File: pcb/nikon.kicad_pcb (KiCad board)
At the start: 2 copper layers, 143.3 x 124.7 mm, 89 parts, among them J1 USB_C_Receptacle_USB2.0, J2 AVR-ISP-6, J3 SJ2-35043A-SMT-TR, SW1 SW_Push, U1 ATmega32U4-AU, Y1 16MHz

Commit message: pre-flippable
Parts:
- J3: value SJ2-35043A-SMT-TR -> SJ2-35894A-SMT-TR; footprint nikon:CUI_SJ2-35043A-SMT-TR -> nikon:CUI_SJ2-35894A-SMT-TR
- MX20: footprint nikon:SW_Kailh_Choc_V1_1.50u -> nikon:SW_Kailh_Choc_V1_1.00u
- moved SW1 18.1 mm to (137.8, 69.6)
- moved D1 8.50 mm to (27.9, 49.7)
- moved D10 8.50 mm to (44.7, 117.7)
- moved D2 8.50 mm to (27.9, 66.7)
- moved D3 8.50 mm to (27.9, 83.7)
- moved D4 8.50 mm to (27.9, 100.7)
- moved D5 8.50 mm to (27.9, 117.7)
- moved D6 8.50 mm to (44.7, 49.7)
- moved D7 8.50 mm to (44.7, 66.7)
- moved D8 8.50 mm to (44.7, 83.7)
- moved D9 8.50 mm to (44.7, 100.7)
- moved MX1 8.50 mm to (35.7, 44.2)
- moved MX10 8.50 mm to (53.7, 112.2)
- moved MX2 8.50 mm to (35.7, 61.2)
- moved MX3 8.50 mm to (35.7, 78.2)
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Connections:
- J3 pad 1: unconnected-(J3-Pad1) -> GND
- J3 pad 2: unconnected-(J3-Pad2) -> /SCL
- J3 pad 3: unconnected-(J3-Pad3) -> /SDA
- J3 pad 4: unconnected-(J3-Pad4) -> +5V
- U1 pad 18: unconnected-(U1-Pad18) -> /SCL
- U1 pad 19: unconnected-(U1-Pad19) -> /SDA
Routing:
- net /D-: track 71.3 -> 0.00 mm
- net /D+: track 69.7 -> 0.00 mm
- net GND: track 27.8 -> 0.00 mm
- net +5V: track 27.0 -> 0.00 mm, vias 2 -> 0
- net Net-(J1-PadB5): track 16.2 -> 0.00 mm, vias 1 -> 0
- net /XTAL1: track 11.7 -> 0.00 mm
- net /XTAL2: track 10.4 -> 0.00 mm
- net /USB_D+: track 10.4 -> 0.00 mm
- net Net-(C1-Pad1): track 9.67 -> 0.00 mm
- net /USB_D-: track 7.61 -> 0.00 mm
- net Net-(F1-Pad2): track 5.77 -> 0.00 mm
- net Net-(D34-Pad2): track 5.27 -> 0.00 mm
- net Net-(D30-Pad2): track 5.26 -> 0.00 mm
- net Net-(D25-Pad2): track 5.25 -> 0.00 mm
- net Net-(J1-PadA5): track 4.50 -> 0.00 mm
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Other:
- board size 143.3 x 124.7 mm -> 143.3 x 128.9 mm

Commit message: ...........
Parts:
- added D35: 1N4148, Diode_SMD:D_SOD-123F, F.Cu at (137.1, 64.6)
- added D36: 1N4148, Diode_SMD:D_SOD-123F, F.Cu at (134.7, 86.4)
- added D37: 1N4148, Diode_SMD:D_SOD-123F, F.Cu at (151.0, 125.3)
- added D38: 1N4148, Diode_SMD:D_SOD-123F, F.Cu at (147.4, 148.6)
- added D39: 1N4148, Diode_SMD:D_SOD-123F, F.Cu at (134.7, 47.6)
- added D40: 1N4148, Diode_SMD:D_SOD-123F, F.Cu at (134.7, 64.6)
- added D41: 1N4148, Diode_SMD:D_SOD-123F, F.Cu at (134.7, 81.6)
- added D42: 1N4148, Diode_SMD:D_SOD-123F, F.Cu at (134.6, 93.8)
- added D43: 1N4148, Diode_SMD:D_SOD-123F, F.Cu at (132.7, 140.1)
- added D44: 1N4148, Diode_SMD:D_SOD-123F, F.Cu at (116.7, 45.4)
- added D45: 1N4148, Diode_SMD:D_SOD-123F, F.Cu at (116.7, 62.4)
- added D46: 1N4148, Diode_SMD:D_SOD-123F, F.Cu at (116.7, 79.4)
- added D47: 1N4148, Diode_SMD:D_SOD-123F, F.Cu at (116.7, 96.4)
- added D48: 1N4148, Diode_SMD:D_SOD-123F, F.Cu at (118.0, 131.6)
- added D49: 1N4148, Diode_SMD:D_SOD-123F, F.Cu at (98.7, 41.2)
- added D50: 1N4148, Diode_SMD:D_SOD-123F, F.Cu at (98.7, 58.2)
- added D51: 1N4148, Diode_SMD:D_SOD-123F, F.Cu at (98.7, 75.2)
- added D52: 1N4148, Diode_SMD:D_SOD-123F, F.Cu at (98.7, 92.2)
- added D53: 1N4148, Diode_SMD:D_SOD-123F, F.Cu at (98.7, 109.2)
- added D54: 1N4148, Diode_SMD:D_SOD-123F, F.Cu at (80.7, 43.3)
- added D55: 1N4148, Diode_SMD:D_SOD-123F, F.Cu at (80.7, 60.3)
- added D56: 1N4148, Diode_SMD:D_SOD-123F, F.Cu at (80.7, 77.3)
- added D57: 1N4148, Diode_SMD:D_SOD-123F, F.Cu at (80.7, 94.3)
- added D58: 1N4148, Diode_SMD:D_SOD-123F, F.Cu at (80.7, 111.3)
- added D59: 1N4148, Diode_SMD:D_SOD-123F, F.Cu at (62.7, 49.7)
- added D60: 1N4148, Diode_SMD:D_SOD-123F, F.Cu at (62.7, 66.7)
- added D61: 1N4148, Diode_SMD:D_SOD-123F, F.Cu at (62.7, 83.7)
- added D62: 1N4148, Diode_SMD:D_SOD-123F, F.Cu at (62.7, 100.7)
- added D63: 1N4148, Diode_SMD:D_SOD-123F, F.Cu at (62.7, 117.7)
- added D64: 1N4148, Diode_SMD:D_SOD-123F, F.Cu at (44.7, 49.7)
- added D65: 1N4148, Diode_SMD:D_SOD-123F, F.Cu at (44.7, 66.7)
- added D66: 1N4148, Diode_SMD:D_SOD-123F, F.Cu at (44.7, 83.7)
- added D67: 1N4148, Diode_SMD:D_SOD-123F, F.Cu at (44.7, 100.7)
- added D68: 1N4148, Diode_SMD:D_SOD-123F, F.Cu at (44.7, 117.7)
- added MX35: MX-NoLED, nikon:SW_Kailh_Choc_V1_1.50u, B.Cu at (143.2, 54.1)
- added MX36: MX-NoLED, nikon:SW_Kailh_Choc_V1_1.50u, B.Cu at (143.2, 81.1)
- added MX37: MX-NoLED, nikon:SW_Kailh_Choc_V1_1.50u, B.Cu at (150.8, 114.8)
- added MX38: MX-NoLED, nikon:SW_Kailh_Choc_V1_1.50u, B.Cu at (147.1, 138.1)
- added MX39: MX-NoLED, nikon:SW_Kailh_Choc_V1_1.00u, B.Cu at (125.7, 42.1)
- added MX40: MX-NoLED, nikon:SW_Kailh_Choc_V1_1.00u, B.Cu at (125.7, 59.1)
- added MX41: MX-NoLED, nikon:SW_Kailh_Choc_V1_1.00u, B.Cu at (125.7, 76.1)
- added MX42: MX-NoLED, nikon:SW_Kailh_Choc_V1_1.00u, B.Cu at (125.7, 93.1)
- added MX43: MX-NoLED, nikon:SW_Kailh_Choc_V1_1.50u, B.Cu at (132.4, 129.6)
- added MX44: MX-NoLED, nikon:SW_Kailh_Choc_V1_1.00u, B.Cu at (107.7, 39.9)
- added MX45: MX-NoLED, nikon:SW_Kailh_Choc_V1_1.00u, B.Cu at (107.7, 56.9)
- added MX46: MX-NoLED, nikon:SW_Kailh_Choc_V1_1.00u, B.Cu at (107.7, 73.9)
- added MX47: MX-NoLED, nikon:SW_Kailh_Choc_V1_1.00u, B.Cu at (107.7, 90.9)
- added MX48: MX-NoLED, nikon:SW_Kailh_Choc_V1_1.50u, B.Cu at (117.6, 121.1)
- added MX49: MX-NoLED, nikon:SW_Kailh_Choc_V1_1.00u, B.Cu at (89.7, 35.7)
- added MX50: MX-NoLED, nikon:SW_Kailh_Choc_V1_1.00u, B.Cu at (89.7, 52.7)
- added MX51: MX-NoLED, nikon:SW_Kailh_Choc_V1_1.00u, B.Cu at (89.7, 69.7)
- added MX52: MX-NoLED, nikon:SW_Kailh_Choc_V1_1.00u, B.Cu at (89.7, 86.7)
- added MX53: MX-NoLED, nikon:SW_Kailh_Choc_V1_1.00u, B.Cu at (89.7, 103.7)
- added MX54: MX-NoLED, nikon:SW_Kailh_Choc_V1_1.00u, B.Cu at (71.7, 37.8)
- added MX55: MX-NoLED, nikon:SW_Kailh_Choc_V1_1.00u, B.Cu at (71.7, 54.8)
- added MX56: MX-NoLED, nikon:SW_Kailh_Choc_V1_1.00u, B.Cu at (71.7, 71.8)
- added MX57: MX-NoLED, nikon:SW_Kailh_Choc_V1_1.00u, B.Cu at (71.7, 88.8)
- added MX58: MX-NoLED, nikon:SW_Kailh_Choc_V1_1.00u, B.Cu at (71.7, 105.8)
- added MX59: MX-NoLED, nikon:SW_Kailh_Choc_V1_1.00u, B.Cu at (53.7, 44.2)
- added MX60: MX-NoLED, nikon:SW_Kailh_Choc_V1_1.00u, B.Cu at (53.7, 61.2)
- added MX61: MX-NoLED, nikon:SW_Kailh_Choc_V1_1.00u, B.Cu at (53.7, 78.2)
- added MX62: MX-NoLED, nikon:SW_Kailh_Choc_V1_1.00u, B.Cu at (53.7, 95.2)
- added MX63: MX-NoLED, nikon:SW_Kailh_Choc_V1_1.00u, B.Cu at (53.7, 112.2)
- added MX64: MX-NoLED, nikon:SW_Kailh_Choc_V1_1.00u, B.Cu at (35.7, 44.2)
- added MX65: MX-NoLED, nikon:SW_Kailh_Choc_V1_1.00u, B.Cu at (35.7, 61.2)
- added MX66: MX-NoLED, nikon:SW_Kailh_Choc_V1_1.00u, B.Cu at (35.7, 78.2)
- added MX67: MX-NoLED, nikon:SW_Kailh_Choc_V1_1.00u, B.Cu at (35.7, 95.2)
- added MX68: MX-NoLED, nikon:SW_Kailh_Choc_V1_1.00u, B.Cu at (35.7, 112.2)
- added R7: 4.7k, Resistor_SMD:R_0805_2012Metric_Pad1.20x1.40mm_HandSolder, F.Cu at (137.9, 69.2)
- added R8: 4.7k, Resistor_SMD:R_0805_2012Metric_Pad1.20x1.40mm_HandSolder, F.Cu at (137.9, 71.5)
- C1, C2, C3, C4, C5, C6, C7, C8, F1, J2, R1, R2, R3, R4, R5, R6, SW1, U1, Y1: moved to F.Cu
- J1: value USB_C_Receptacle_USB2.0 -> USB4105-GF-A; footprint nikon:USB_C_GCT_USB4085 -> nikon:GCT_USB4105-GF-A; moved to F.Cu
- J3: value SJ2-35894A-SMT-TR -> SJ2-35954A-SMT-TR; footprint nikon:CUI_SJ2-35894A-SMT-TR -> nikon:CUI_SJ2-35954A-SMT-TR; moved to F.Cu
- moved J2 49.8 mm to (113.6, 104.0), turned to 180 degrees
- moved SW1 48.4 mm to (103.7, 103.9), turned to 0 degrees
- moved C3 26.0 mm to (121.7, 103.1), turned to 0 degrees
- moved R6 20.1 mm to (140.1, 117.3), turned to 0 degrees
- moved C5 18.1 mm to (125.0, 105.5), turned to -90 degrees
- moved Y1 17.3 mm to (121.7, 109.3), turned to 90 degrees
- moved C7 16.8 mm to (141.8, 113.2), turned to 90 degrees
- moved C1 16.0 mm to (134.0, 98.4), turned to 180 degrees
- moved R1 13.6 mm to (136.0, 37.5), turned to 90 degrees
- moved C4 13.3 mm to (133.1, 100.7), turned to 0 degrees
- moved C2 8.83 mm to (125.0, 112.1), turned to 90 degrees
- moved C8 6.73 mm to (141.8, 106.0), turned to -90 degrees
- moved R4 6.14 mm to (149.0, 37.5), turned to -90 degrees
- moved C6 3.20 mm to (127.7, 117.4), turned to 180 degrees
- moved J1 2.61 mm to (143.2, 27.8), turned to 180 degrees
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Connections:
- net /Col1 renamed /LCol1
- net /Col2 renamed /LCol2
- net /Col3 renamed /LCol3
- net /Col4 renamed /LCol4
- net /Col5 renamed /LCol5
- net /Col6 renamed /LCol6
- net /Col7 renamed /LCol7
- net /Row1 renamed /LRow1
- net /Row2 renamed /LRow2
- net /Row3 renamed /LRow3
- net /Row4 renamed /LRow4
- net /Row5 renamed /LRow5
- J1 pad A5: Net-(J1-PadA5) -> Net-(R4-Pad1)
- R2 pad 1: /D- -> /USB_D-
- R2 pad 2: /USB_D- -> /D-
- R3 pad 1: /D+ -> /USB_D+
- R3 pad 2: /USB_D+ -> /D+
- R4 pad 1: GND -> Net-(R4-Pad1)
- R4 pad 2: Net-(J1-PadA5) -> GND
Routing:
- net /LRow5: track 0.00 -> 140.4 mm
- net /LRow3: track 0.00 -> 123.9 mm, vias 0 -> 2
- net +5V: track 0.00 -> 123.7 mm, vias 0 -> 6
- net /LRow2: track 0.00 -> 122.2 mm
- net /RRow2: track 0.00 -> 101.3 mm
- net /RRow3: track 0.00 -> 100.9 mm
- net /RRow1: track 0.00 -> 99.0 mm
- net /RRow4: track 0.00 -> 99.0 mm
- net /LRow4: track 0.00 -> 97.7 mm
- net /LRow1: track 0.00 -> 97.4 mm
- net /LCol3: track 0.00 -> 77.3 mm, vias 0 -> 8
- net /LCol4: track 0.00 -> 76.2 mm, vias 0 -> 8
- net /LCol2: track 0.00 -> 74.5 mm, vias 0 -> 8
- net /LCol1: track 0.00 -> 74.5 mm
- net /D-: track 0.00 -> 73.1 mm
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- added copper zone on F.Cu, net GND
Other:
- outline, holes or cut-outs redrawn

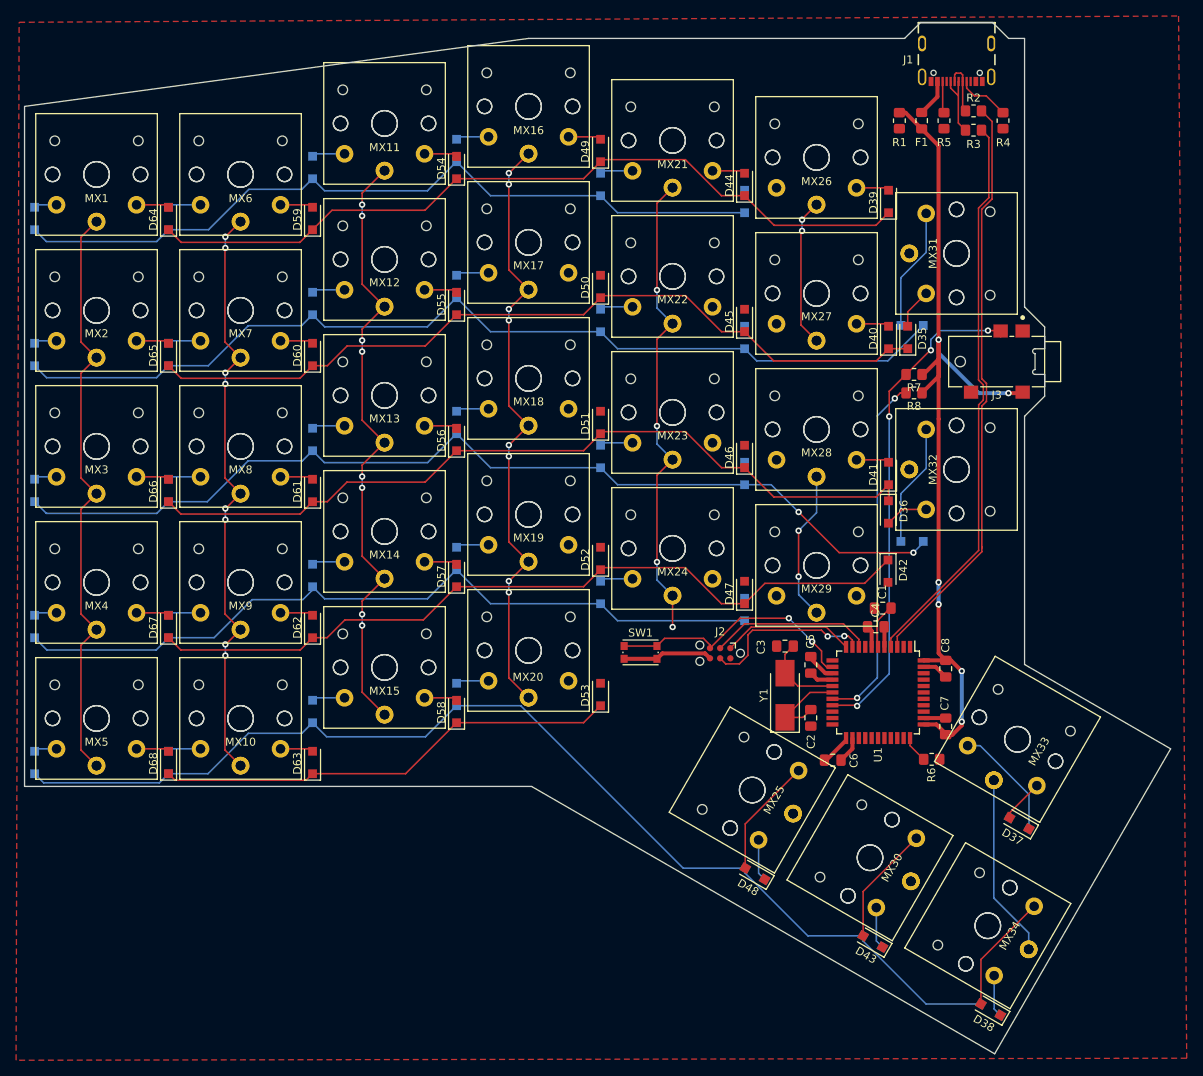
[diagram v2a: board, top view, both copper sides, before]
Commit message: remove right pcb
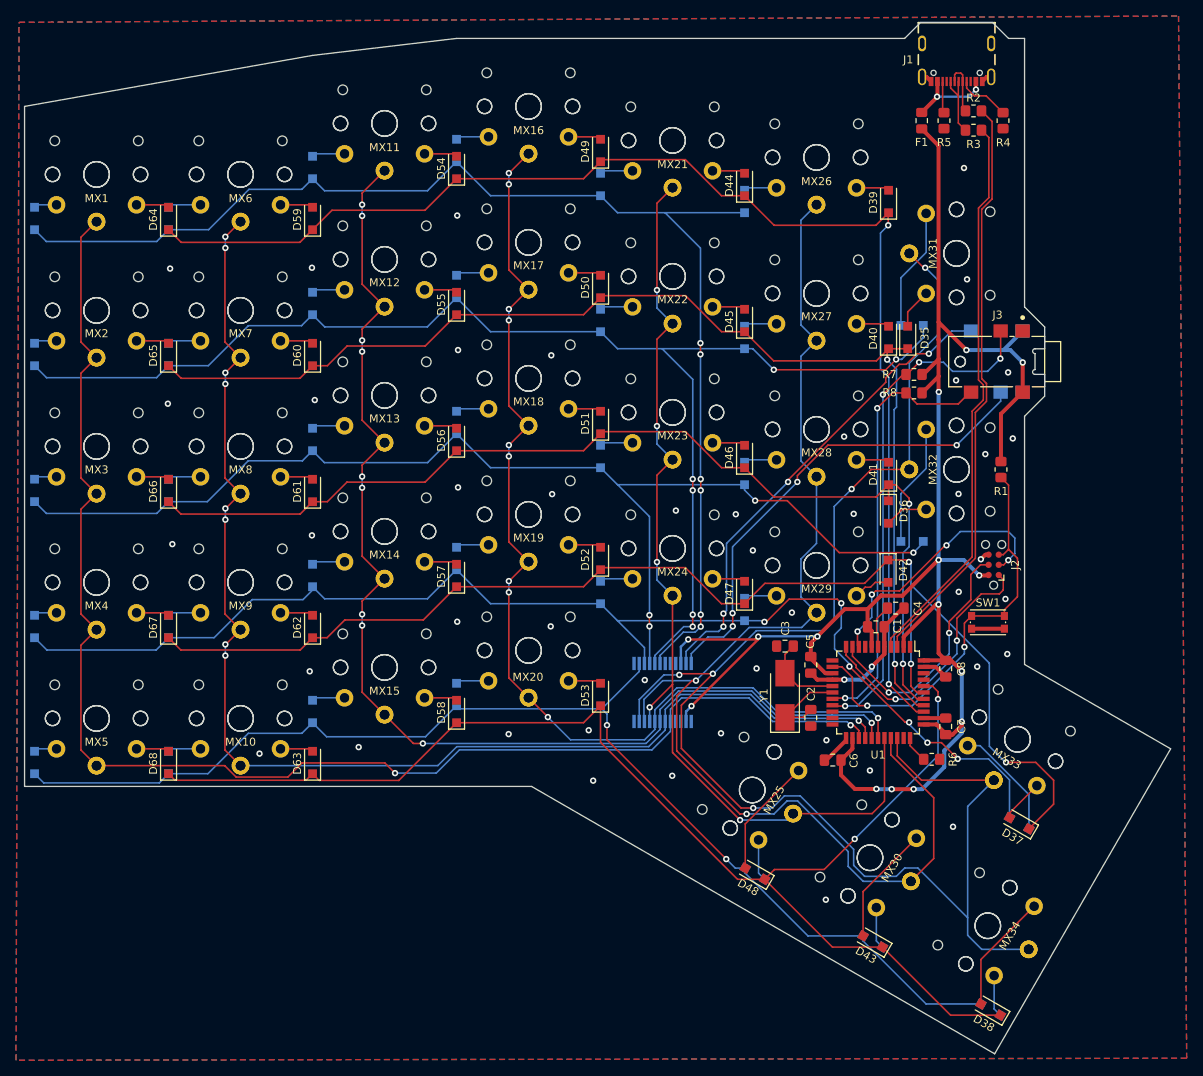
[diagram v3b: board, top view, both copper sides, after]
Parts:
- added J4: SJ2-35954A-SMT-TR, nikon:CUI_SJ2-35954A-SMT-TR, B.Cu at (148.2, 67.6)
- added U2: MCP23018-E/SS, nikon:MCP23018-E&slash_SS, B.Cu at (106.5, 108.9)
- moved R1 45.4 mm to (148.7, 81.1)
- moved SW1 43.6 mm to (147.1, 100.2)
- moved J2 35.9 mm to (147.8, 93.0), turned to 90 degrees
- moved C1 1.63 mm to (135.6, 98.4), turned to 0 degrees
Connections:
- net /SCL renamed /RSCL
- net /SDA renamed /RSDA
- U1 pad 25: unconnected-(U1-Pad25) -> /LCol1
- U1 pad 26: unconnected-(U1-Pad26) -> /LCol2
- U1 pad 27: unconnected-(U1-Pad27) -> /LCol3
- U1 pad 28: unconnected-(U1-Pad28) -> /LCol4
- U1 pad 29: unconnected-(U1-Pad29) -> /LCol5
- U1 pad 30: unconnected-(U1-Pad30) -> /LCol6
- U1 pad 31: unconnected-(U1-Pad31) -> /LCol7
- U1 pad 36: unconnected-(U1-Pad36) -> /RRow1
- U1 pad 37: unconnected-(U1-Pad37) -> /RRow2
- U1 pad 38: unconnected-(U1-Pad38) -> /RRow3
- U1 pad 39: unconnected-(U1-Pad39) -> /RRow4
- U1 pad 40: unconnected-(U1-Pad40) -> /RRow5
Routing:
- net /LCol7: track 22.9 -> 190.3 mm, vias 0 -> 5
- net /LCol6: track 37.5 -> 153.7 mm, vias 4 -> 2
- net /RRow5: track 58.2 -> 165.7 mm, vias 0 -> 2
- net /LCol1: track 74.5 -> 179.8 mm, vias 0 -> 2
- net +5V: track 123.7 -> 226.6 mm, vias 6 -> 15
- net /LCol2: track 74.5 -> 160.9 mm, vias 8 -> 9
- net /LCol3: track 77.3 -> 147.4 mm, vias 8 -> 10
- net /RRow1: track 99.0 -> 164.5 mm, vias 0 -> 2
- net /RRow4: track 99.0 -> 160.6 mm, vias 0 -> 3
- net /LRow1: track 97.4 -> 158.5 mm, vias 0 -> 6
- net /LSDA: track 0.00 -> 60.5 mm, vias 0 -> 4
- net /LCol5: track 59.8 -> 120.1 mm, vias 4 -> 5
- net /LSCL: track 0.00 -> 60.1 mm, vias 0 -> 4
- net /LRow4: track 97.7 -> 157.7 mm, vias 0 -> 6
- net /LCol4: track 76.2 -> 130.3 mm, vias 8 -> 10
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- added copper zone on B.Cu, net GND
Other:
- outline, holes or cut-outs redrawn

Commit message: 1.0
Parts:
- added G***: LOGO, nikon:full_logo_35mm_mirrored, F.Cu at (163.3, 32.6)
- added G***: LOGO, nikon:full_logo_35mm, B.Cu at (163.3, 32.6)
- moved C1 46.4 mm to (181.9, 99.1)
- moved C6 46.4 mm to (174.1, 118.1)
- moved C7 46.4 mm to (188.2, 113.9)
- moved C8 46.4 mm to (188.2, 106.7)
- moved D30 46.4 mm to (179.1, 140.8)
- moved D34 46.4 mm to (193.8, 149.3)
- moved D38 46.4 mm to (193.8, 149.3)
- moved D43 46.4 mm to (179.1, 140.8)
- moved J1 46.4 mm to (189.6, 28.6)
- moved R2 46.4 mm to (191.7, 37.0)
- moved R3 46.4 mm to (191.7, 39.4)
- moved R4 46.4 mm to (195.4, 38.2)
- moved R6 46.4 mm to (186.4, 118.0)
- moved R7 46.4 mm to (184.2, 69.9)
- moved R8 46.4 mm to (184.2, 72.3)
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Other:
- board text added: "RESET"
- board text added: "htpkbs.com"
- board text added: "nikon v1.0"

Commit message: esd
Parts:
- added C9: 0.1u, Capacitor_SMD:C_0805_2012Metric_Pad1.18x1.45mm_HandSolder, F.Cu at (264.1, 102.4)
- moved C6 80.9 mm to (255.0, 117.4)
- moved C5 80.1 mm to (251.3, 100.4), turned to 0 degrees
- moved C8 71.8 mm to (260.0, 105.9)
- moved C3 71.5 mm to (239.6, 103.1)
- moved Y1 71.5 mm to (239.6, 109.2)
- moved C2 71.5 mm to (242.8, 112.1)
- moved U1 71.5 mm to (251.3, 108.9)
- moved C7 71.5 mm to (259.7, 113.1)
- moved C1 71.5 mm to (253.4, 97.2)
- moved R6 70.4 mm to (256.7, 121.5)
- moved C4 69.8 mm to (249.1, 97.2)
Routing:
- net /LCol7: track 190.3 -> 0.00 mm, vias 5 -> 0
- net /LCol1: track 179.8 -> 0.00 mm, vias 2 -> 0
- net +5V: track 226.6 -> 55.9 mm, vias 15 -> 0
- net /LRow2: track 167.6 -> 0.00 mm, vias 6 -> 0
- net /RRow5: track 165.7 -> 0.00 mm, vias 2 -> 0
- net /RRow1: track 164.5 -> 0.00 mm, vias 2 -> 0
- net /LCol2: track 160.9 -> 0.00 mm, vias 9 -> 0
- net /RRow4: track 160.6 -> 0.00 mm, vias 3 -> 0
- net /LRow1: track 158.5 -> 0.00 mm, vias 6 -> 0
- net /LRow4: track 157.7 -> 0.00 mm, vias 6 -> 0
- net /LCol6: track 153.7 -> 0.00 mm, vias 2 -> 0
- net /LRow5: track 149.9 -> 0.00 mm, vias 2 -> 0
- net /RRow2: track 148.4 -> 0.00 mm, vias 2 -> 0
- net /LRow3: track 148.3 -> 0.00 mm, vias 4 -> 0
- net /LCol3: track 147.4 -> 0.00 mm, vias 10 -> 0
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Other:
- board size 143.3 x 128.9 mm -> 142.7 x 128.4 mm
